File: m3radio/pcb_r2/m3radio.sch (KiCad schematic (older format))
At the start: 47 parts, among them IC1 NCP380, IC101 STM32F405RxTx, IC102 MCP2562, IC2 NC7SZ04, IC3 CS2100-CP, IC4 SL18860DC, IC5 MAX_M8Q, IC6 SN74LVC1G0832, J101 WEST TOP, J102 WEST BOT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

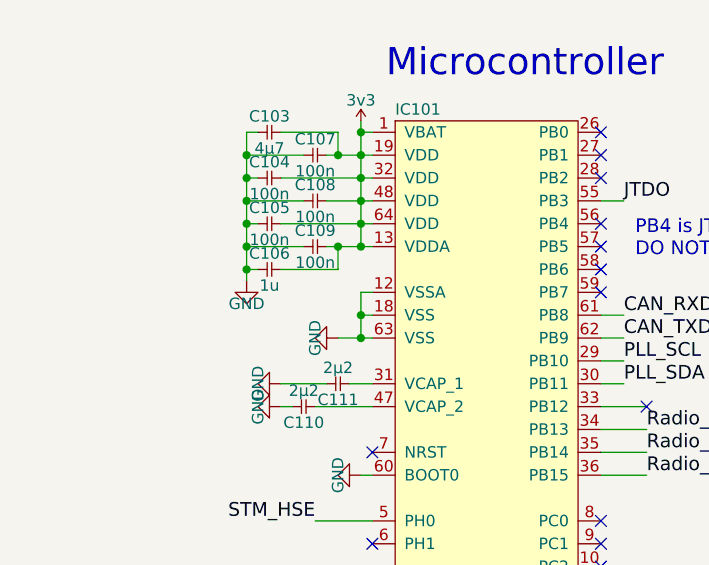
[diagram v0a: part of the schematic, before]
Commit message: Add potential divider and small changes to radio pcb
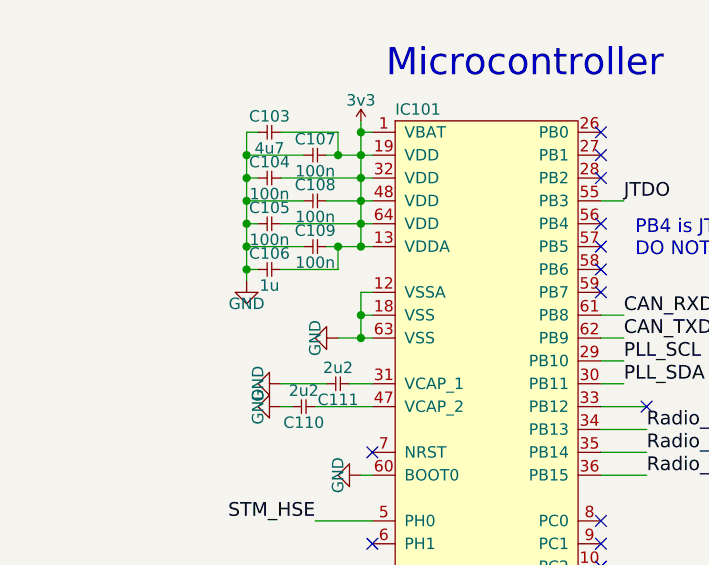
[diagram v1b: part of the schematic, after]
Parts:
- C103: value 4µ7 -> 4u7
- C110, C111: value 2µ2 -> 2u2
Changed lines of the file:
@@
 LIBS:TOAD-cache
 LIBS:max-8q
+LIBS:m3radio-rescue
 LIBS:m3radio-cache
 EELAYER 26 0
@@
 P 1500 2050
 F 0 "C111" H 1550 2120 50  0000 C CNN
-F 1 "2µ2" H 1550 1980 50  0000 C CNN
+F 1 "2u2" H 1550 1980 50  0000 C CNN
 F 2 "agg:0402" H 1500 2050 50  0001 C CNN
 F 3 "" H 1500 2050 50  0001 C CNN
@@
 P 1350 2150
 F 0 "C110" H 1400 2220 50  0000 C CNN
-F 1 "2µ2" H 1400 2080 50  0000 C CNN
+F 1 "2u2" H 1400 2080 50  0000 C CNN
 F 2 "agg:0402" H 1350 2150 50  0001 C CNN
 F 3 "" H 1350 2150 50  0001 C CNN
@@
 P 1100 950
 F 0 "C103" H 1150 1020 50  0000 C CNN
-F 1 "4µ7" H 1150 880 50  0000 C CNN
+F 1 "4u7" H 1150 880 50  0000 C CNN
 F 2 "agg:0402" H 1100 950 50  0001 C CNN
 F 3 "" H 1100 950 50  0001 C CNN
@@
 Connection ~ 4500 6150
 Wire Wire Line
-	4450 6150 4550 6150
-Wire Wire Line
 	5500 6150 5500 6100
 Wire Wire Line
@@
 	1600 3250 1350 3250
 NoConn ~ 2800 2150
+Wire Wire Line
+	4450 6150 4550 6150
 $EndSCHEMATC
